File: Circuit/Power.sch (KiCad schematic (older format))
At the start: 15 parts, among them Q201 FDN340P, Q202 FDN340P, Q203 FDN340P, U201 CN3063, U202 MCP6002

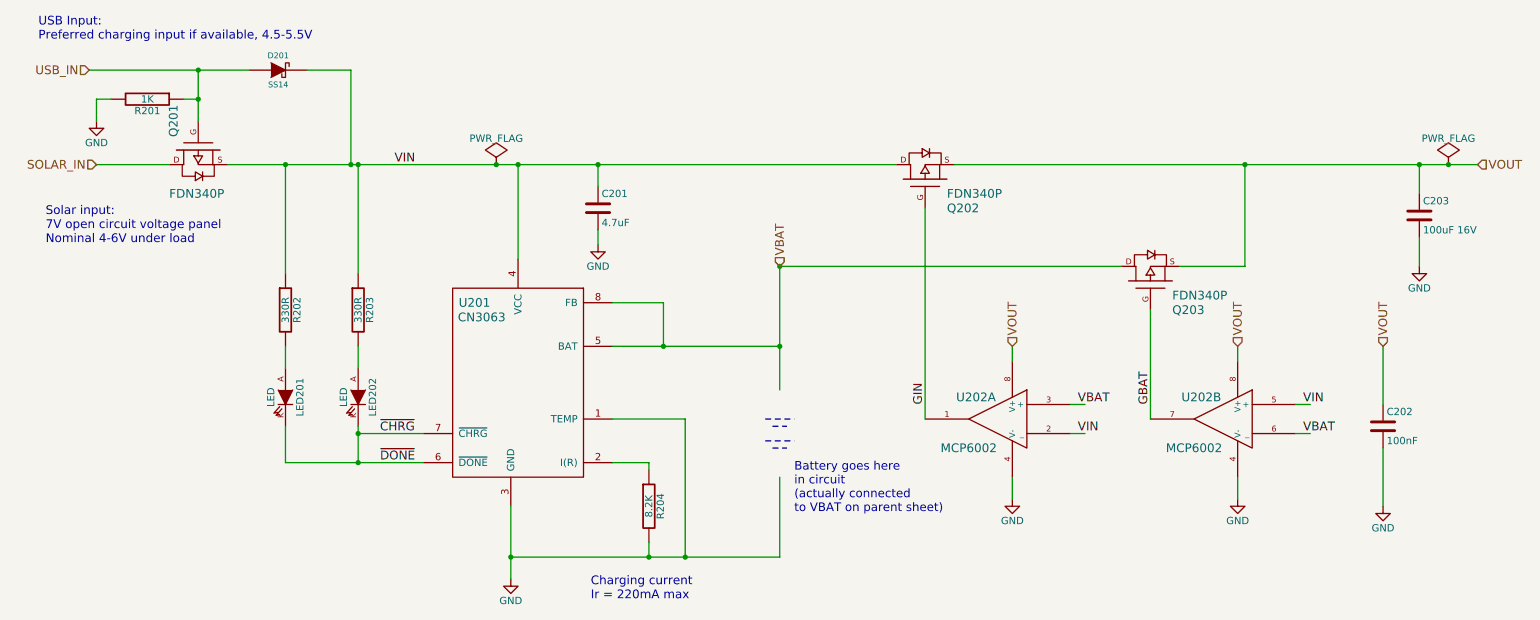
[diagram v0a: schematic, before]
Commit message: Footprint assignment for schematic, including footprints for new parts
Removed on-PCB UV sensor in favour of offboard one.
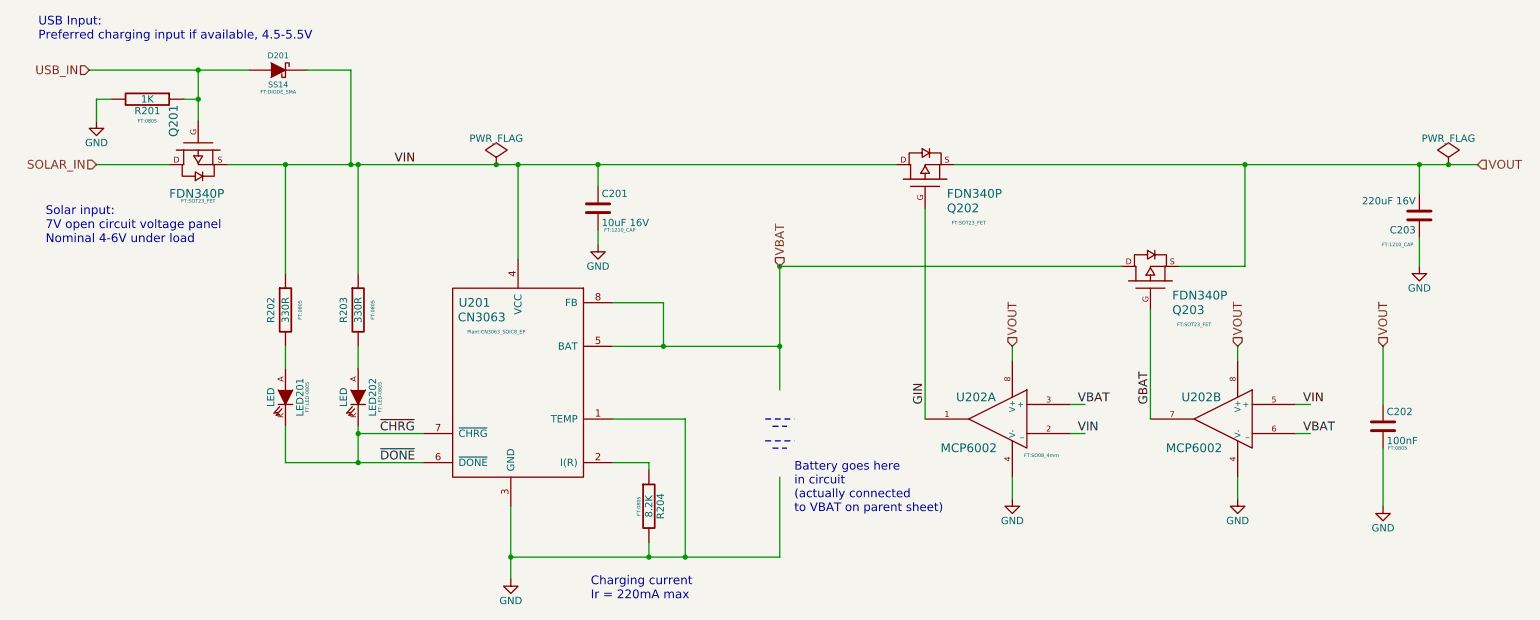
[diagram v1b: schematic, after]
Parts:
- C201: value 4.7uF -> 10uF 16V; footprint (none) -> FT:1210_CAP
- C202, R201, R202, R203, R204: footprint (none) -> FT:0805
- C203: value 100uF 16V -> 220uF 16V; footprint (none) -> FT:1210_CAP
- D201: footprint (none) -> FT:DIODE_SMA
- LED201, LED202: footprint (none) -> FT:LED-0805
- Q201, Q202, Q203: footprint (none) -> FT:SOT23_FET
- U201: footprint (none) -> Plant:CN3063_SOIC8_EP
- U202: footprint (none) -> FT:SO08_4mm
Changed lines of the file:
@@
 F 0 "U201" H 3750 3750 60  0000 C CNN
 F 1 "CN3063" H 3800 3650 60  0000 C CNN
-F 2 "" H 3800 2900 60  0000 C CNN
+F 2 "Plant:CN3063_SOIC8_EP" H 3900 3550 24  0000 C CNN
 F 3 "" H 3800 2900 60  0000 C CNN
 	1    4050 3250
@@
 SOLAR_IN
 $Comp
-L GND #PWR029
+L GND #PWR036
 U 1 1 563C4E24
 P 4000 4650
-F 0 "#PWR029" H 4000 4400 50  0001 C CNN
+F 0 "#PWR036" H 4000 4400 50  0001 C CNN
 F 1 "GND" H 4000 4500 50  0000 C CNN
 F 2 "" H 4000 4650 60  0000 C CNN
@@
 F 0 "R204" V 5030 4150 50  0000 C CNN
 F 1 "8.2K" V 4950 4150 50  0000 C CNN
-F 2 "" V 4880 4150 30  0000 C CNN
+F 2 "FT:0805" V 4880 4150 24  0000 C CNN
 F 3 "" H 4950 4150 30  0000 C CNN
 	1    4950 4150
@@
 F 0 "Q201" H 1760 1870 60  0000 R CNN
 F 1 "FDN340P" V 2150 1900 60  0000 R CNN
-F 2 "" H 1850 1700 60  0000 C CNN
+F 2 "FT:SOT23_FET" V 2200 1700 24  0000 C CNN
 F 3 "" H 1850 1700 60  0000 C CNN
 	1    1850 1700
@@
 F 0 "D201" H 2400 1250 40  0000 C CNN
 F 1 "SS14" H 2400 1050 40  0000 C CNN
-F 2 "" H 2400 1150 60  0000 C CNN
+F 2 "FT:DIODE_SMA" H 2400 1000 24  0000 C CNN
 F 3 "" H 2400 1150 60  0000 C CNN
 	1    2400 1150
@@
 F 0 "R201" V 1580 1350 50  0000 C CNN
 F 1 "1K" V 1500 1350 50  0000 C CNN
-F 2 "" H 1500 1350 60  0000 C CNN
+F 2 "FT:0805" V 1650 1350 24  0000 C CNN
 F 3 "" H 1500 1350 60  0000 C CNN
 	1    1500 1350
@@
 $EndComp
 $Comp
-L GND #PWR030
+L GND #PWR037
 U 1 1 563C5B2C
 P 1150 1500
-F 0 "#PWR030" H 1150 1250 50  0001 C CNN
+F 0 "#PWR037" H 1150 1250 50  0001 C CNN
 F 1 "GND" H 1150 1350 50  0000 C CNN
 F 2 "" H 1150 1500 60  0000 C CNN
@@
 F 0 "LED202" H 2950 3500 50  0000 C CNN
 F 1 "LED" H 2950 3300 50  0000 C CNN
-F 2 "" H 2950 3400 60  0000 C CNN
+F 2 "FT:LED-0805" H 2950 3550 24  0000 C CNN
 F 3 "" H 2950 3400 60  0000 C CNN
 	1    2950 3400
@@
 U 1 1 563C6031
 P 2950 2800
-F 0 "R203" V 3030 2800 50  0000 C CNN
+F 0 "R203" V 2850 2800 50  0000 C CNN
 F 1 "330R" V 2950 2800 50  0000 C CNN
-F 2 "" H 2950 2800 60  0000 C CNN
+F 2 "FT:0805" V 3050 2800 24  0000 C CNN
 F 3 "" H 2950 2800 60  0000 C CNN
 	1    2950 2800
@@
 F 0 "LED201" H 2450 3500 50  0000 C CNN
 F 1 "LED" H 2450 3300 50  0000 C CNN
-F 2 "" H 2450 3400 60  0000 C CNN
+F 2 "FT:LED-0805" H 2450 3550 24  0000 C CNN
 F 3 "" H 2450 3400 60  0000 C CNN
 	1    2450 3400
@@
 U 1 1 563FF8B7
 P 2450 2800
-F 0 "R202" V 2530 2800 50  0000 C CNN
+F 0 "R202" V 2350 2800 50  0000 C CNN
 F 1 "330R" V 2450 2800 50  0000 C CNN
-F 2 "" H 2450 2800 60  0000 C CNN
+F 2 "FT:0805" V 2550 2800 24  0000 C CNN
 F 3 "" H 2450 2800 60  0000 C CNN
 	1    2450 2800
@@
 F 0 "Q202" V 6650 1750 60  0000 R CNN
 F 1 "FDN340P" V 6750 1750 60  0000 R CNN
-F 2 "" H 6850 1900 60  0000 C CNN
+F 2 "FT:SOT23_FET" V 6550 1600 24  0000 C CNN
 F 3 "" H 6850 1900 60  0000 C CNN
 	1    6850 1900
@@
 Charging current\nIr = 220mA max
 $Comp
-L GND #PWR031
+L GND #PWR038
 U 1 1 56417FB3
 P 7450 4100
-F 0 "#PWR031" H 7450 3850 50  0001 C CNN
+F 0 "#PWR038" H 7450 3850 50  0001 C CNN
 F 1 "GND" H 7450 3950 50  0000 C CNN
 F 2 "" H 7450 4100 60  0000 C CNN
@@
 F 0 "Q203" V 8200 2450 60  0000 R CNN
 F 1 "FDN340P" V 8300 2450 60  0000 R CNN
-F 2 "" H 8400 2600 60  0000 C CNN
+F 2 "FT:SOT23_FET" V 8100 2300 24  0000 C CNN
 F 3 "" H 8400 2600 60  0000 C CNN
 	1    8400 2600
@@
 VOUT
 $Comp
-L GND #PWR032
+L GND #PWR039
 U 1 1 5641AA9F
 P 10250 2500
-F 0 "#PWR032" H 10250 2250 50  0001 C CNN
+F 0 "#PWR039" H 10250 2250 50  0001 C CNN
 F 1 "GND" H 10250 2350 50  0000 C CNN
 F 2 "" H 10250 2500 60  0000 C CNN
@@
 F 0 "U202" H 7500 3700 60  0000 C CNN
 F 1 "MCP6002" H 7550 3350 60  0000 C CNN
-F 2 "" H 7350 3550 60  0000 C CNN
+F 2 "FT:SO08_4mm" H 7050 3300 24  0000 C CNN
 F 3 "" H 7350 3550 60  0000 C CNN
 	1    7350 3550
@@
 VOUT
 $Comp
-L GND #PWR033
+L GND #PWR040
 U 1 1 5642C1C1
 P 9000 4100
-F 0 "#PWR033" H 9000 3850 50  0001 C CNN
+F 0 "#PWR040" H 9000 3850 50  0001 C CNN
 F 1 "GND" H 9000 3950 50  0000 C CNN
 F 2 "" H 9000 4100 60  0000 C CNN
@@
 P 10250 2150
 F 0 "C203" H 10275 2250 50  0000 L CNN
-F 1 "100uF 16V" H 10275 2050 50  0000 L CNN
-F 2 "" H 10288 2000 30  0000 C CNN
+F 1 "220uF 16V" H 10275 2050 50  0000 L CNN
+F 2 "FT:1210_CAP" H 10400 2350 24  0000 C CNN
 F 3 "" H 10250 2150 60  0000 C CNN
 	1    10250 2150
-	1    0    0    -1
-$EndComp
-$Comp
-L PWR_FLAG #FLG034
+	-1   0    0    1
+$EndComp
+$Comp
+L PWR_FLAG #FLG041
 U 1 1 5642D1CE
 P 10450 1800
-F 0 "#FLG034" H 10450 1895 50  0001 C CNN
+F 0 "#FLG041" H 10450 1895 50  0001 C CNN
 F 1 "PWR_FLAG" H 10450 1980 50  0000 C CNN
 F 2 "" H 10450 1800 60  0000 C CNN
@@
 $EndComp
 $Comp
-L PWR_FLAG #FLG035
+L PWR_FLAG #FLG042
 U 1 1 5642D5A3
 P 3900 1800
-F 0 "#FLG035" H 3900 1895 50  0001 C CNN
+F 0 "#FLG042" H 3900 1895 50  0001 C CNN
 F 1 "PWR_FLAG" H 3900 1980 50  0000 C CNN
 F 2 "" H 3900 1800 60  0000 C CNN
@@
 F 0 "C202" H 10025 3700 50  0000 L CNN
 F 1 "100nF" H 10025 3500 50  0000 L CNN
-F 2 "" H 10038 3450 30  0000 C CNN
+F 2 "FT:0805" H 10100 3450 24  0000 C CNN
 F 3 "" H 10000 3600 60  0000 C CNN
 	1    10000 3600
@@
 $EndComp
 $Comp
-L GND #PWR036
+L GND #PWR043
 U 1 1 5642DA26
 P 10000 4150
-F 0 "#PWR036" H 10000 3900 50  0001 C CNN
+F 0 "#PWR043" H 10000 3900 50  0001 C CNN
 F 1 "GND" H 10000 4000 50  0000 C CNN
 F 2 "" H 10000 4150 60  0000 C CNN
@@
 P 4600 2100
 F 0 "C201" H 4625 2200 50  0000 L CNN
-F 1 "4.7uF" H 4625 2000 50  0000 L CNN
-F 2 "" H 4638 1950 30  0000 C CNN
+F 1 "10uF 16V" H 4625 2000 50  0000 L CNN
+F 2 "FT:1210_CAP" H 4750 1950 24  0000 C CNN
 F 3 "" H 4600 2100 60  0000 C CNN
 	1    4600 2100
@@
 $EndComp
 $Comp
-L GND #PWR037
+L GND #PWR044
 U 1 1 5642CE9D
 P 4600 2350
-F 0 "#PWR037" H 4600 2100 50  0001 C CNN
+F 0 "#PWR044" H 4600 2100 50  0001 C CNN
 F 1 "GND" H 4600 2200 50  0000 C CNN
 F 2 "" H 4600 2350 60  0000 C CNN

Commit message: Updated footprints for connectors
Removed Surplus power.
Added connectors for soil sensor.
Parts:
- U202: footprint (none) -> FT:SO08_4mm
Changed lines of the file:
@@
 SOLAR_IN
 $Comp
-L GND #PWR036
+L GND #PWR032
 U 1 1 563C4E24
 P 4000 4650
-F 0 "#PWR036" H 4000 4400 50  0001 C CNN
+F 0 "#PWR032" H 4000 4400 50  0001 C CNN
 F 1 "GND" H 4000 4500 50  0000 C CNN
 F 2 "" H 4000 4650 60  0000 C CNN
@@
 $EndComp
 $Comp
-L GND #PWR037
+L GND #PWR033
 U 1 1 563C5B2C
 P 1150 1500
-F 0 "#PWR037" H 1150 1250 50  0001 C CNN
+F 0 "#PWR033" H 1150 1250 50  0001 C CNN
 F 1 "GND" H 1150 1350 50  0000 C CNN
 F 2 "" H 1150 1500 60  0000 C CNN
@@
 Charging current\nIr = 220mA max
 $Comp
-L GND #PWR038
+L GND #PWR034
 U 1 1 56417FB3
 P 7450 4100
-F 0 "#PWR038" H 7450 3850 50  0001 C CNN
+F 0 "#PWR034" H 7450 3850 50  0001 C CNN
 F 1 "GND" H 7450 3950 50  0000 C CNN
 F 2 "" H 7450 4100 60  0000 C CNN
@@
 VOUT
 $Comp
-L GND #PWR039
+L GND #PWR035
 U 1 1 5641AA9F
 P 10250 2500
-F 0 "#PWR039" H 10250 2250 50  0001 C CNN
+F 0 "#PWR035" H 10250 2250 50  0001 C CNN
 F 1 "GND" H 10250 2350 50  0000 C CNN
 F 2 "" H 10250 2500 60  0000 C CNN
@@
 F 0 "U202" H 9050 3700 60  0000 C CNN
 F 1 "MCP6002" H 9100 3350 60  0000 C CNN
-F 2 "" H 8900 3550 60  0000 C CNN
+F 2 "FT:SO08_4mm" H 8900 3550 60  0001 C CNN
 F 3 "" H 8900 3550 60  0000 C CNN
 	2    8900 3550
@@
 VOUT
 $Comp
-L GND #PWR040
+L GND #PWR036
 U 1 1 5642C1C1
 P 9000 4100
-F 0 "#PWR040" H 9000 3850 50  0001 C CNN
+F 0 "#PWR036" H 9000 3850 50  0001 C CNN
 F 1 "GND" H 9000 3950 50  0000 C CNN
 F 2 "" H 9000 4100 60  0000 C CNN
@@
 $EndComp
 $Comp
-L PWR_FLAG #FLG041
+L PWR_FLAG #FLG037
 U 1 1 5642D1CE
 P 10450 1800
-F 0 "#FLG041" H 10450 1895 50  0001 C CNN
+F 0 "#FLG037" H 10450 1895 50  0001 C CNN
 F 1 "PWR_FLAG" H 10450 1980 50  0000 C CNN
 F 2 "" H 10450 1800 60  0000 C CNN
@@
 $EndComp
 $Comp
-L PWR_FLAG #FLG042
+L PWR_FLAG #FLG038
 U 1 1 5642D5A3
 P 3900 1800
-F 0 "#FLG042" H 3900 1895 50  0001 C CNN
+F 0 "#FLG038" H 3900 1895 50  0001 C CNN
 F 1 "PWR_FLAG" H 3900 1980 50  0000 C CNN
 F 2 "" H 3900 1800 60  0000 C CNN
@@
 $EndComp
 $Comp
-L GND #PWR043
+L GND #PWR039
 U 1 1 5642DA26
 P 10000 4150
-F 0 "#PWR043" H 10000 3900 50  0001 C CNN
+F 0 "#PWR039" H 10000 3900 50  0001 C CNN
 F 1 "GND" H 10000 4000 50  0000 C CNN
 F 2 "" H 10000 4150 60  0000 C CNN
@@
 $EndComp
 $Comp
-L GND #PWR044
+L GND #PWR040
 U 1 1 5642CE9D
 P 4600 2350
-F 0 "#PWR044" H 4600 2100 50  0001 C CNN
+F 0 "#PWR040" H 4600 2100 50  0001 C CNN
 F 1 "GND" H 4600 2200 50  0000 C CNN
 F 2 "" H 4600 2350 60  0000 C CNN

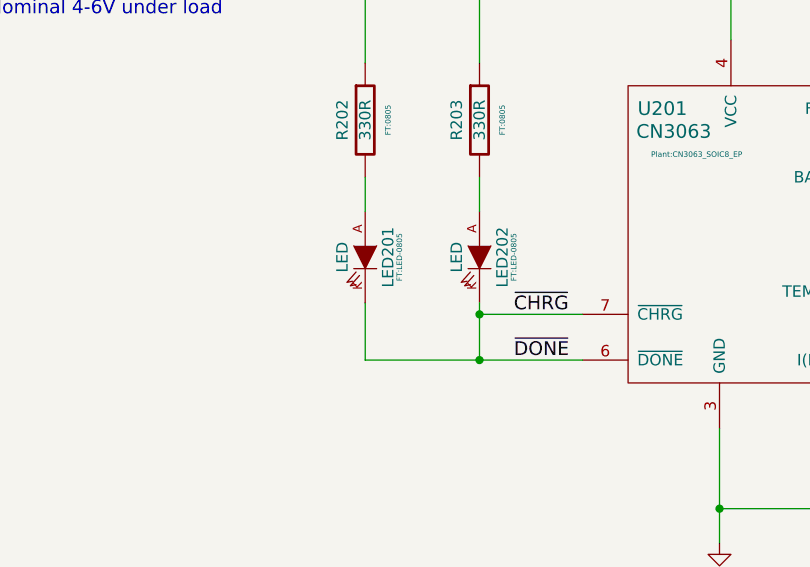
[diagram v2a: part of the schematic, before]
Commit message: Fixed Charge LED's
They were accidentally linked.
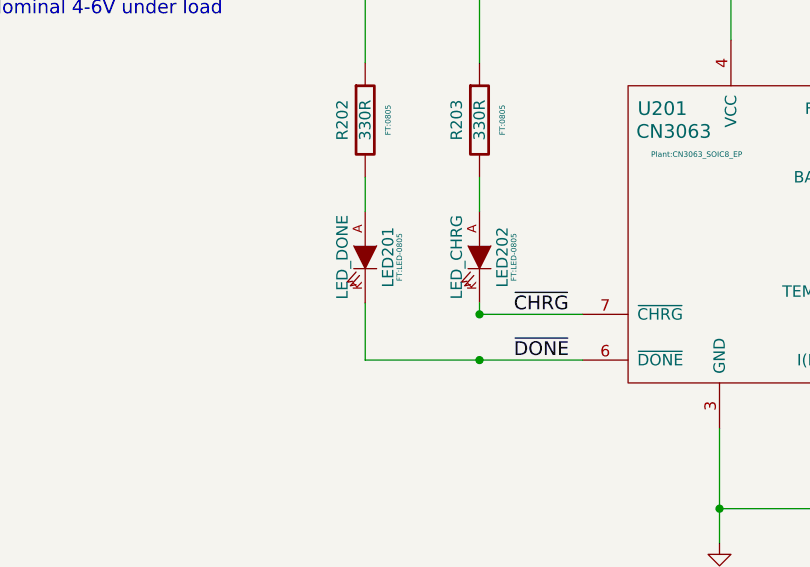
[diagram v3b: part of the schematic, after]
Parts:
- LED201: value LED -> LED_DONE
- LED202: value LED -> LED_CHRG
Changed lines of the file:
@@
 P 2950 3400
 F 0 "LED202" H 2950 3500 50  0000 C CNN
-F 1 "LED" H 2950 3300 50  0000 C CNN
+F 1 "LED_CHRG" H 2950 3300 50  0000 C CNN
 F 2 "FT:LED-0805" H 2950 3550 24  0000 C CNN
 F 3 "" H 2950 3400 60  0000 C CNN
@@
 P 2450 3400
 F 0 "LED201" H 2450 3500 50  0000 C CNN
-F 1 "LED" H 2450 3300 50  0000 C CNN
+F 1 "LED_DONE" H 2450 3300 50  0000 C CNN
 F 2 "FT:LED-0805" H 2450 3550 24  0000 C CNN
 F 3 "" H 2450 3400 60  0000 C CNN
@@
 	2950 2550 2950 1800
 Connection ~ 2950 1800
-Wire Wire Line
-	2950 3600 2950 3850
 Connection ~ 2950 3650
 Wire Wire Line
@@
 Text Notes 5950 4200 0    59   ~ 0
 Battery goes here\nin circuit\n(actually connected\nto VBAT on parent sheet)
+Wire Wire Line
+	2950 3600 2950 3650
 $EndSCHEMATC

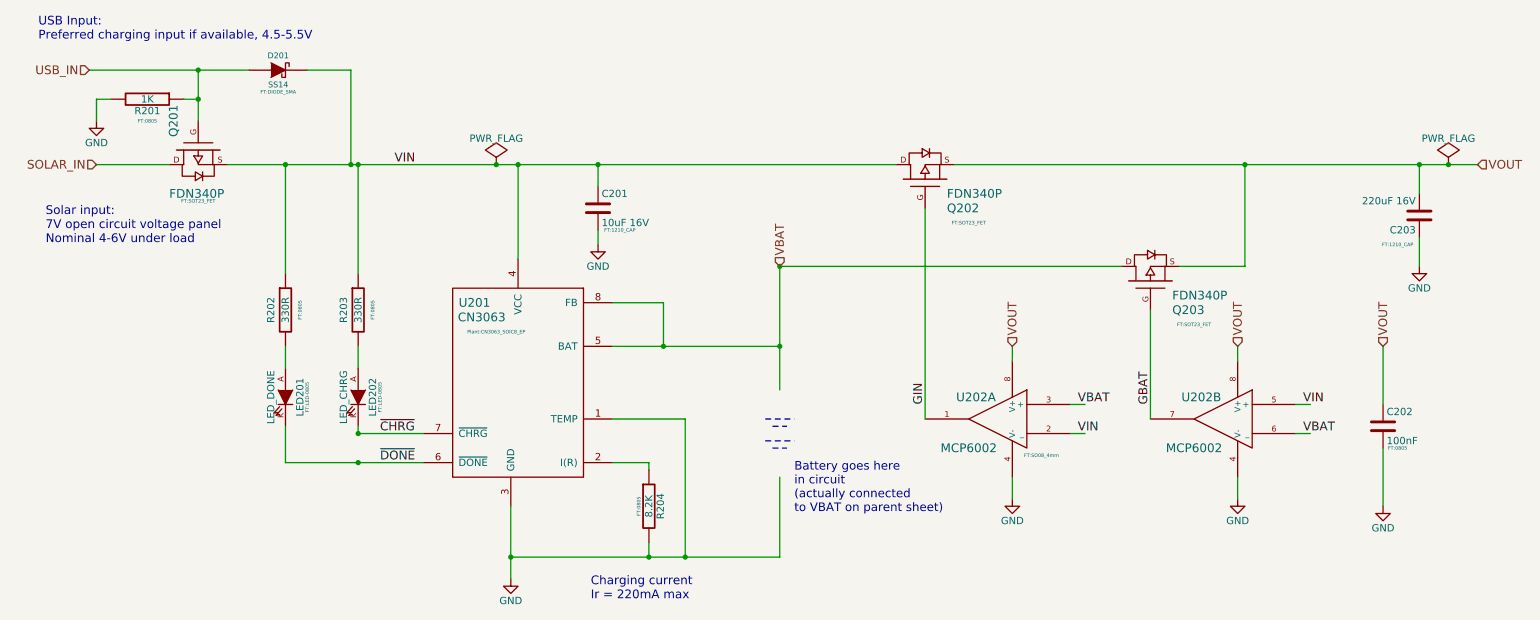
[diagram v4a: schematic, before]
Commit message: Revise schematic for V1.1 based on V1.0 evaluation:
* Swap SDA, SCL on ESP (5,4 to 4,5) to match Arduino default
* Q101 source, drain were swapped
* BME280 change i2c address config  0x76 -> 0x77 (match Adafruit library)
* ADXL345 change i2c address from 0x1d -> 0x53 (match Adafruit library)
* Specify colours for "charging", "done" LEDs in component values
* R202, R203 LED series resistors changed to 1K
* Add GPIO2 pullup to strapping resistors, required for reliable reset
* Add autoreset: connect ESP_RESET to PA7 on STM32, GPIO0 to PB8. Remove
  "ADC5" pin from design.
* Add 1K series resistor between GPIO16 and RESET (replacing solder
  jumper). Otherwise pulling reset line draws >50mA!!
* Add 1K series resistor from GPIO0 to GPIO0 reset button & STM32
  GPIO. This is because GPIO0 defaults to clock output on reset,
  driving a square wave.
* Change 220uF 1210 bulk capacitor value to 100uF, reflecting part
  availability and reliability shown in testing.
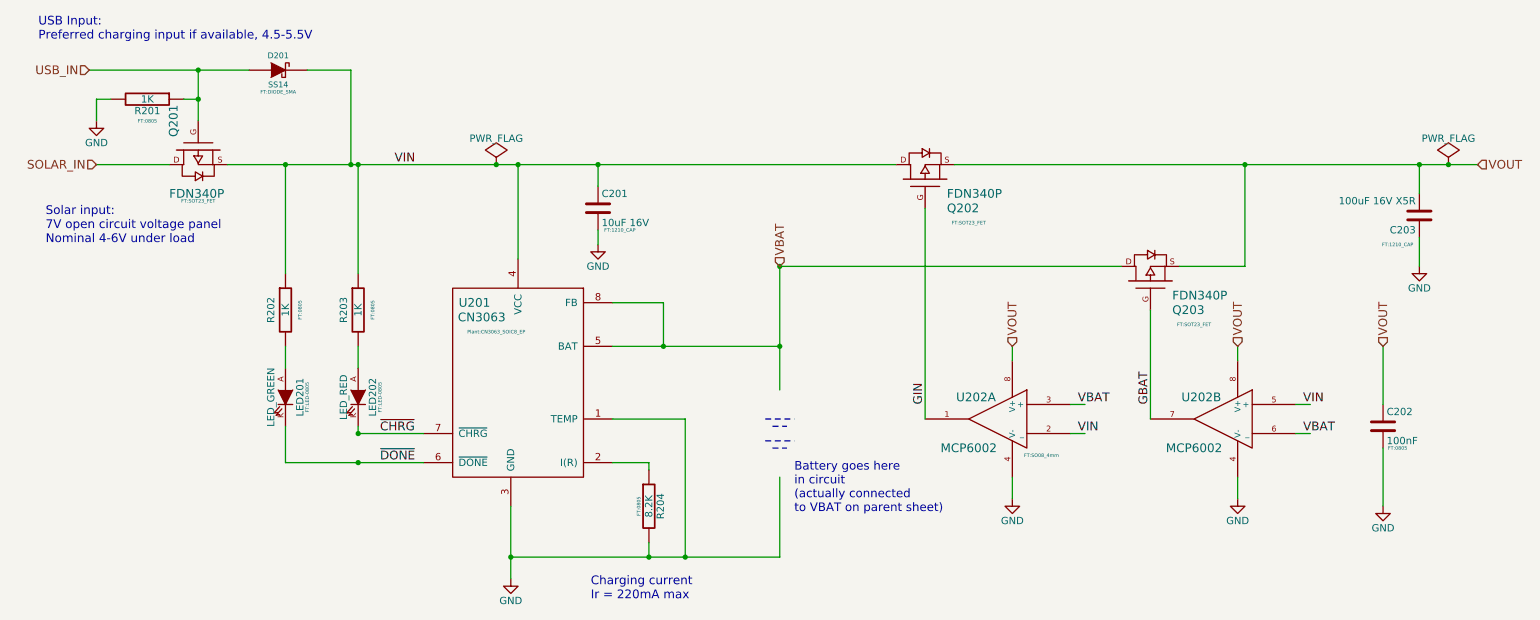
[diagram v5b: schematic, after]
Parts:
- C203: value 220uF 16V -> 100uF 16V X5R
- LED201: value LED_DONE -> LED_GREEN
- LED202: value LED_CHRG -> LED_RED
- R202, R203: value 330R -> 1K
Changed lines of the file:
@@
 P 2950 3400
 F 0 "LED202" H 2950 3500 50  0000 C CNN
-F 1 "LED_CHRG" H 2950 3300 50  0000 C CNN
+F 1 "LED_RED" H 2950 3300 50  0000 C CNN
 F 2 "FT:LED-0805" H 2950 3550 24  0000 C CNN
 F 3 "" H 2950 3400 60  0000 C CNN
@@
 P 2950 2800
 F 0 "R203" V 2850 2800 50  0000 C CNN
-F 1 "330R" V 2950 2800 50  0000 C CNN
+F 1 "1K" V 2950 2800 50  0000 C CNN
 F 2 "FT:0805" V 3050 2800 24  0000 C CNN
 F 3 "" H 2950 2800 60  0000 C CNN
@@
 P 2450 3400
 F 0 "LED201" H 2450 3500 50  0000 C CNN
-F 1 "LED_DONE" H 2450 3300 50  0000 C CNN
+F 1 "LED_GREEN" H 2450 3300 50  0000 C CNN
 F 2 "FT:LED-0805" H 2450 3550 24  0000 C CNN
 F 3 "" H 2450 3400 60  0000 C CNN
@@
 P 2450 2800
 F 0 "R202" V 2350 2800 50  0000 C CNN
-F 1 "330R" V 2450 2800 50  0000 C CNN
+F 1 "1K" V 2450 2800 50  0000 C CNN
 F 2 "FT:0805" V 2550 2800 24  0000 C CNN
 F 3 "" H 2450 2800 60  0000 C CNN
@@
 P 10250 2150
 F 0 "C203" H 10275 2250 50  0000 L CNN
-F 1 "220uF 16V" H 10275 2050 50  0000 L CNN
+F 1 "100uF 16V X5R" H 10275 2050 50  0000 L CNN
 F 2 "FT:1210_CAP" H 10400 2350 24  0000 C CNN
 F 3 "" H 10250 2150 60  0000 C CNN
